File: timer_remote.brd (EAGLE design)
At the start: 64 x 80 mm, 27 parts, among them J1 120VAC, J2 Low Volt Relay, K1 G5LE-14-DC5, K2 G5LE-14-DC5, Q1 DMN2053UVT

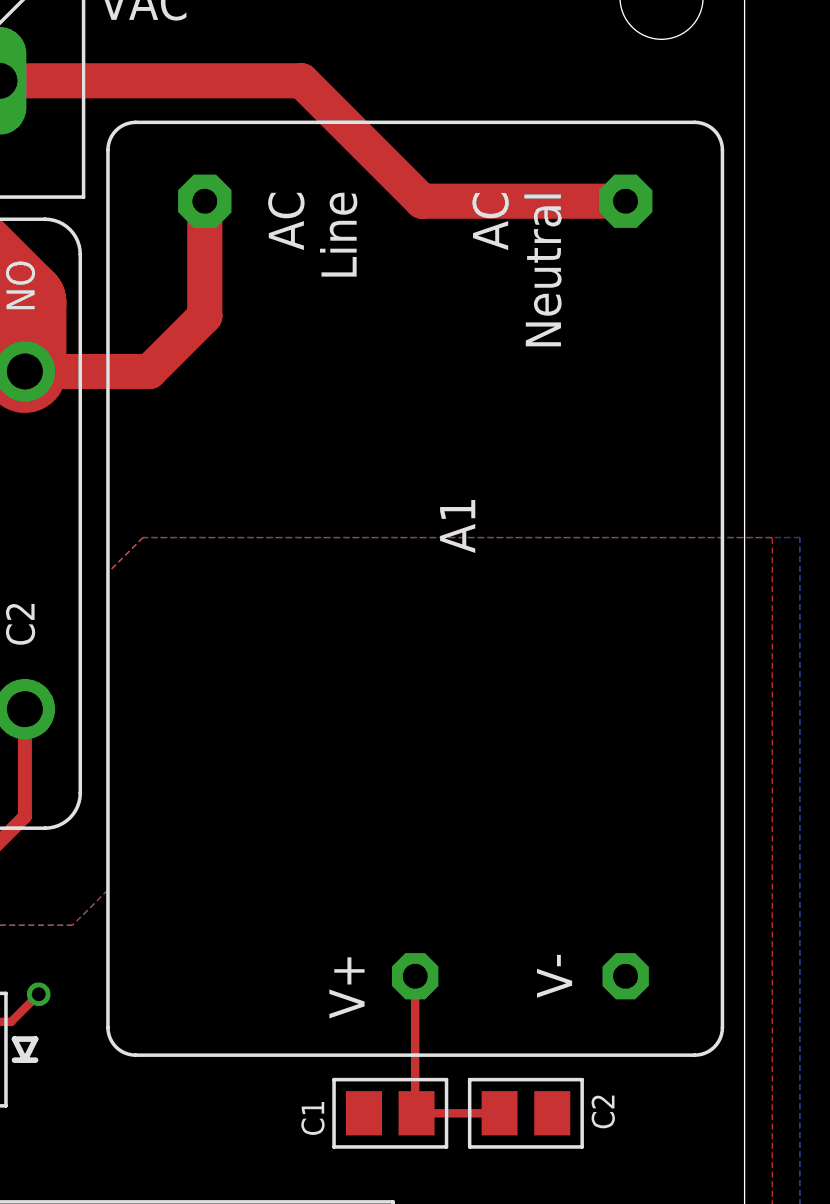
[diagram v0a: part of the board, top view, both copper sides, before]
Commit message: Minor tweaks to PCB traces, update README, BoM, images.
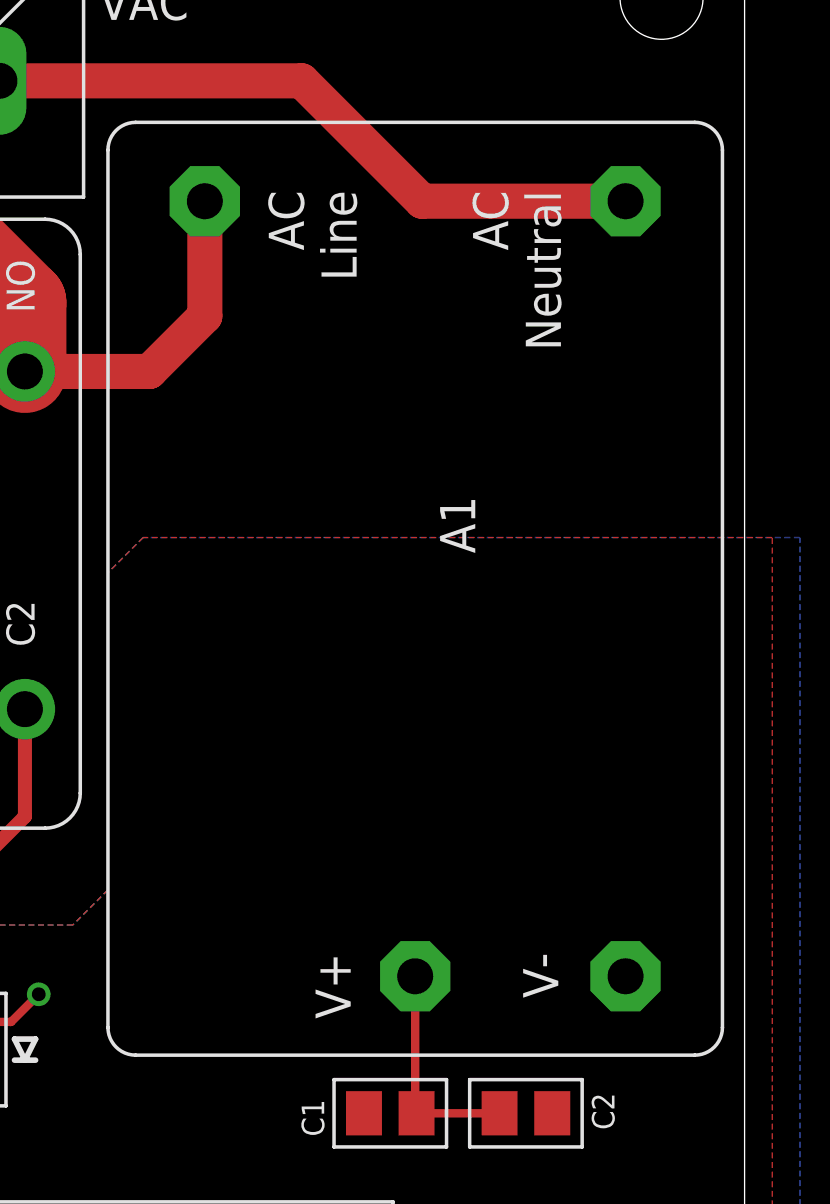
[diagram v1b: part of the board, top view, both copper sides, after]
